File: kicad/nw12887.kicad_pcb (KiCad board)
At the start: 2 copper layers, 18.3 x 31.1 mm, 4 parts, among them U1 ds12887, U2 ds12887, Y1 Crystal_Small

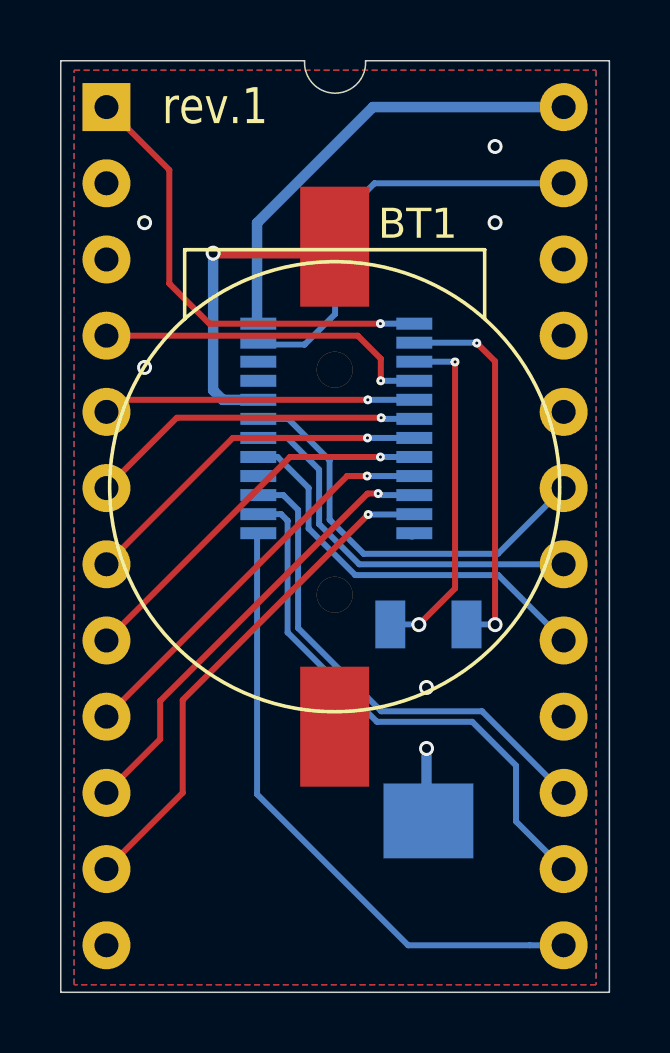
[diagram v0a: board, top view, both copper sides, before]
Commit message: Replaced BQ3285 by bigger SO version
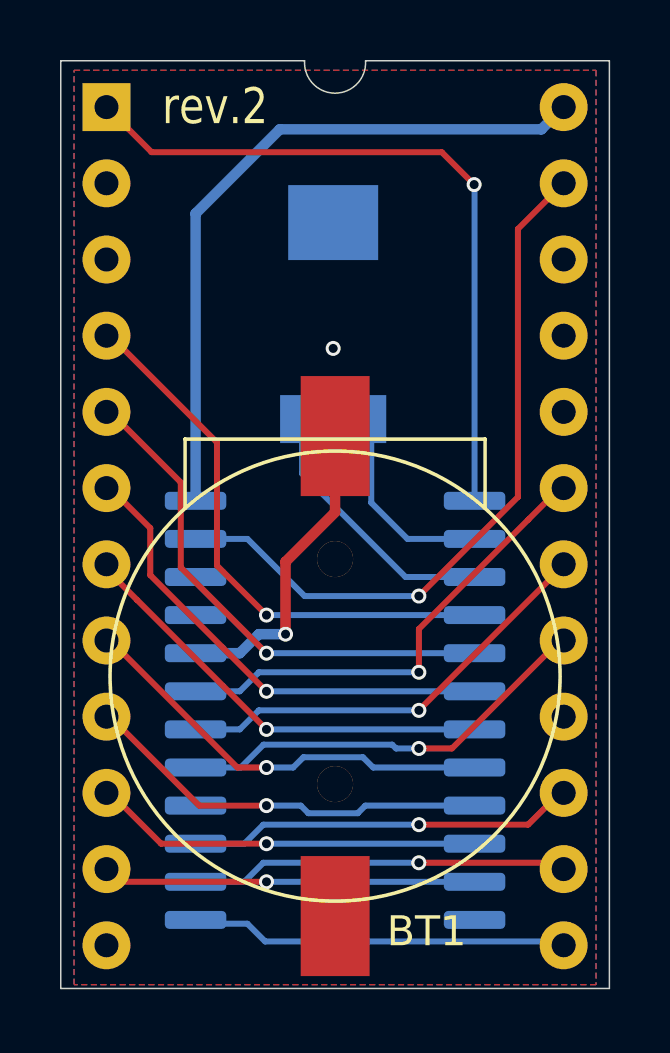
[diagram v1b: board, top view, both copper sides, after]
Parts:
- U2: footprint Package_SO:SSOP-24_3.9x8.7mm_P0.635mm -> Package_SO:SOIC-24W_7.5x15.4mm_P1.27mm
- moved Y1 14.2 mm to (134.6, 86.4), turned to 0 degrees
- moved U2 9.40 mm to (134.6, 99.6)
- moved BT1 6.31 mm to (134.6, 98.4)
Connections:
- Y1 pad 1: X1 -> X2
- Y1 pad 2: X2 -> X1
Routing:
- net SQW: track 14.3 -> 24.0 mm, vias 0 -> 1
- net CS: track 21.0 -> 12.5 mm
- net MOT: track 15.4 -> 23.9 mm
- net VCC: track 15.1 -> 23.3 mm
- net AD0: track 11.3 -> 18.6 mm
- net AD1: track 10.4 -> 17.3 mm
- net X1: track 12.7 -> 6.73 mm, vias 2 -> 0
- net AS: track 18.4 -> 12.6 mm, vias 0 -> 1
- net AD2: track 11.2 -> 16.0 mm
- net AD7: track 16.9 -> 12.5 mm
- net RW: track 16.6 -> 13.2 mm, vias 0 -> 1
- net AD3: track 12.0 -> 14.8 mm
- net X2: track 11.6 -> 9.09 mm, vias 2 -> 0
- net GND: track 2.25 -> 0.00 mm, vias 6 -> 1
- net AD6: track 15.1 -> 13.0 mm
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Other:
- board size 18.3 x 31.1 mm -> 18.3 x 30.9 mm
- board text added: "rev.2"
- board text removed: "rev.1"
